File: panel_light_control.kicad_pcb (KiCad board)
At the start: 4 copper layers, 109 parts, among them J1 Conn_01x02, J11 RJ45_Shielded, J12 RJ45_Shielded, J13 HR911105A, J6 Conn_01x04, Q1 IRF540N, Q2 IRF540N, Q3 IRF540N, U1 L7805, U2 LM324, U3 STM32F207VGTx, U4 MCP2562-E-P, U5 LAN8720A, Y1 Crystal_GND24

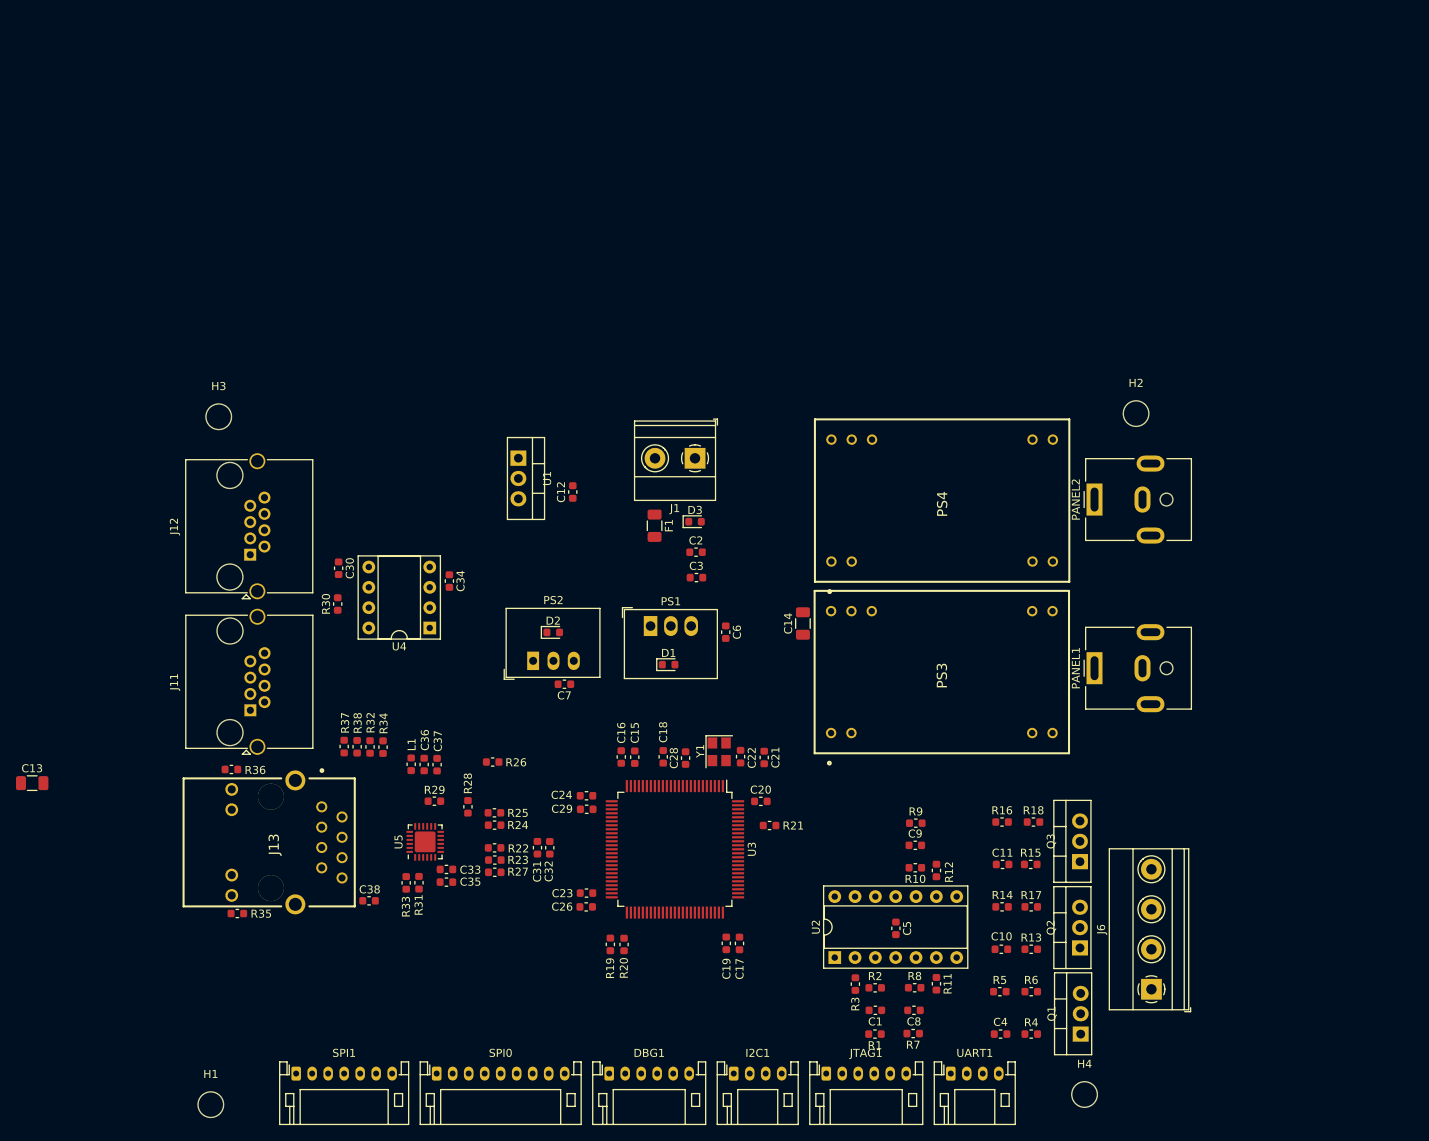
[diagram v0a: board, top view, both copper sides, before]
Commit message: PHY routing done? Current sink routing is back to square one (yay fwd annotations)
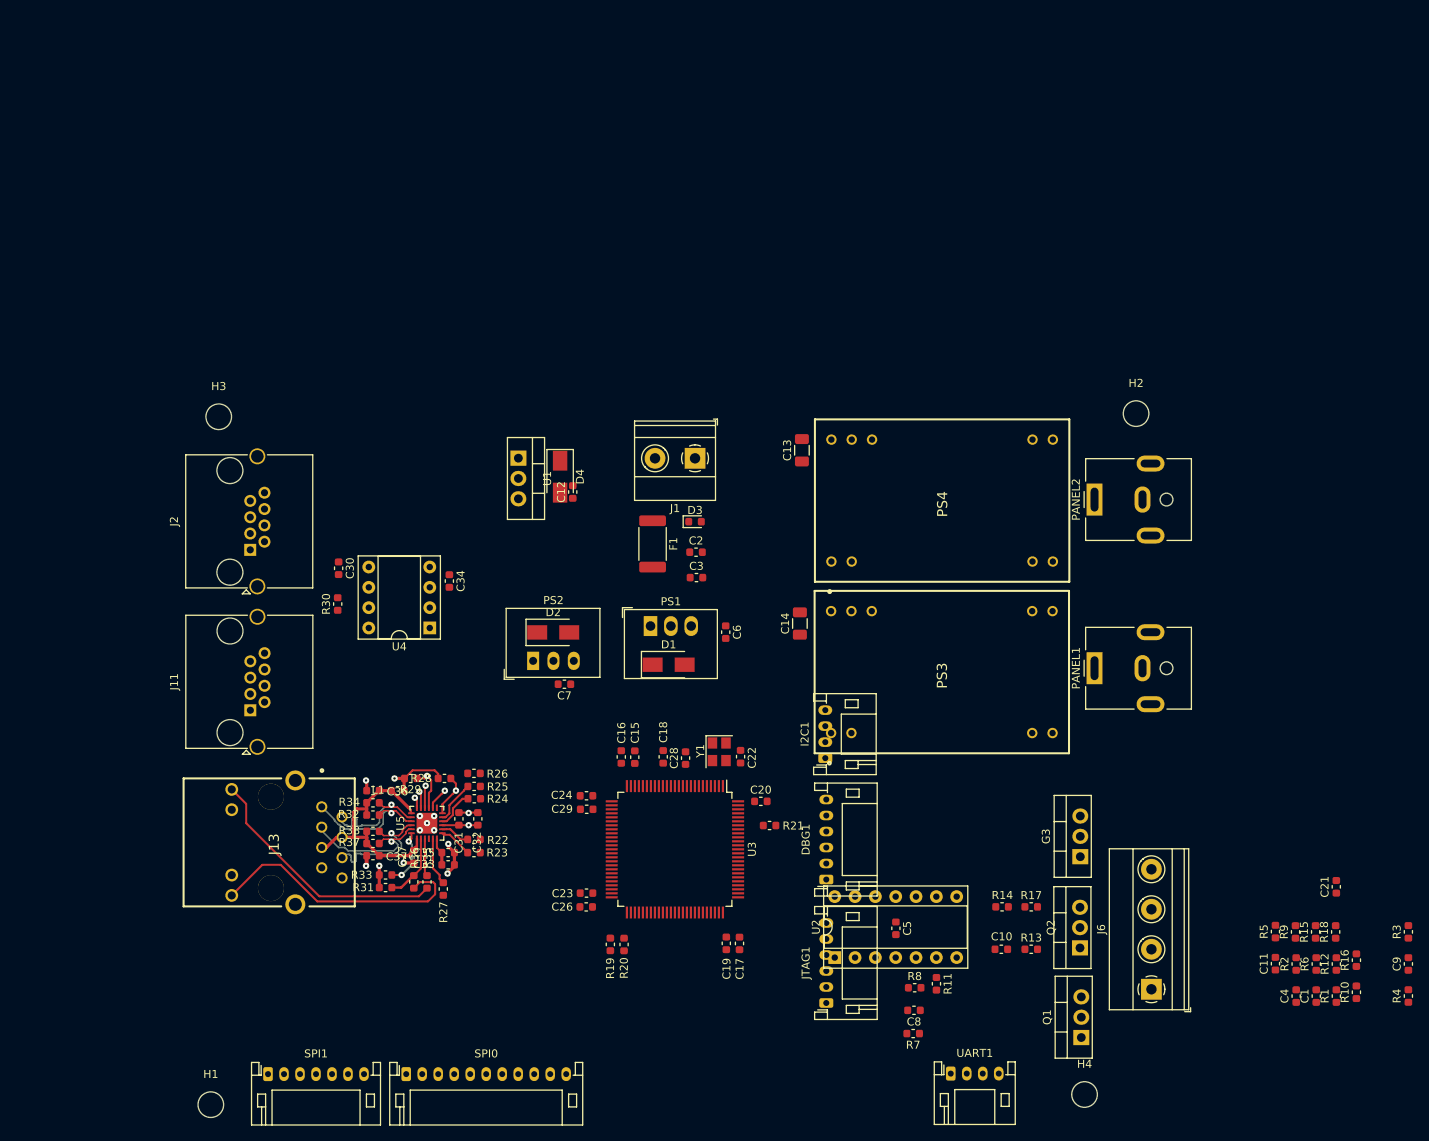
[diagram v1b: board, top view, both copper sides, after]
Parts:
- removed C38: 22nF, Capacitor_SMD:C_0603_1608Metric
- removed J12: RJ45_Shielded, Connector_RJ:RJ45_Amphenol_RJHSE5380
- removed Q3: IRF540N, Package_TO_SOT_THT:TO-220-3_Vertical
- added C27: 100nF, Capacitor_SMD:C_0603_1608Metric, F.Cu at (82.8, 129.9)
- added D4: D, Diode_SMD:D_SMA, F.Cu at (101.1, 82.4)
- added G3: IRF540N, Package_TO_SOT_THT:TO-220-3_Vertical, F.Cu at (166.1, 129.9)
- added J2: RJ45_Shielded, Connector_RJ:RJ45_Amphenol_RJHSE5380, F.Cu at (62.4, 91.6)
- C36, C37: value 104pF -> 100nF
- D1, D2: footprint Diode_SMD:D_0603_1608Metric -> Diode_SMD:D_SMA
- F1: footprint Fuse:Fuse_1206_3216Metric -> Fuse:Fuse_2512_6332Metric
- L1: value L -> FB
- SPI0: value Conn_01x09 -> Conn_01x10; footprint Connector_JST:JST_PH_S9B-PH-K_1x09_P2.00mm_Horizontal -> Connector_JST:JST_PH_S11B-PH-K_1x11_P2.00mm_Horizontal
- U3: value STM32F207VGTx -> STM32F207VGT6
- moved C13 104.8 mm to (131.3, 79.1), turned to 90 degrees
- moved C21 73.3 mm to (198.1, 133.7), turned to 90 degrees
- moved R3 69.4 mm to (207.1, 139.3), turned to 90 degrees
- moved C9 63.4 mm to (207.1, 143.3), turned to 90 degrees
- moved R1 57.9 mm to (198.1, 147.3), turned to 90 degrees
- moved R10 57.3 mm to (200.6, 146.9), turned to 90 degrees
- moved C1 55.1 mm to (195.6, 147.3), turned to 90 degrees
- moved R2 52.7 mm to (193.1, 143.3), turned to 90 degrees
- moved R12 51.3 mm to (198.1, 143.3)
- moved R9 49.4 mm to (193.0, 139.3), turned to 90 degrees
- moved R16 47.5 mm to (200.6, 142.9), turned to 90 degrees
- moved R4 47.4 mm to (207.1, 147.3), turned to 90 degrees
- moved I2C1 41.1 mm to (134.2, 117.6), turned to 90 degrees
- moved R18 40.2 mm to (198.0, 139.3), turned to 90 degrees
- moved C4 37.3 mm to (193.1, 147.3), turned to 90 degrees
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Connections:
- net /MCU/RX_N renamed RX_N
- net /MCU/RX_P renamed RX_P
- net /MCU/TX_N renamed TX_N
- net /MCU/TX_P renamed TX_P
- C21 pad 1: GND -> Net-(C21-Pad1)
- C21 pad 2: Net-(C21-Pad2) -> GND
- C31 pad 1: +3.3V -> GND
- C31 pad 2: GND -> +3.3V
- C32 pad 1: +3.3V -> GND
- C32 pad 2: GND -> +3.3V
- C33 pad 1: Net-(C33-Pad1) -> GND
- C33 pad 2: GND -> /MCU/VDDCR
- C35 pad 1: Net-(C33-Pad1) -> GND
- C35 pad 2: GND -> /MCU/VDDCR
- C36 pad 1: VDDA -> GND
- C36 pad 2: GND -> PHY_VDDA
- C37 pad 1: VDDA -> GND
- C37 pad 2: GND -> PHY_VDDA
- J13 pad 4: VDDA -> PHY_VDDA
- J13 pad 5: VDDA -> PHY_VDDA
- L1 pad 1: +3.3V -> PHY_VDDA
- L1 pad 2: VDDA -> +3.3V
- R1 pad 1: PWM_R -> Net-(C1-Pad2)
- R1 pad 2: Net-(C1-Pad2) -> PWM_R
- R14 pad 1: Net-(Q2-Pad3) -> Net-(C10-Pad2)
- R14 pad 2: Net-(C10-Pad2) -> Net-(Q2-Pad3)
- R16 pad 1: Net-(Q3-Pad3) -> Net-(C11-Pad2)
- R16 pad 2: Net-(C11-Pad2) -> Net-(G3-Pad3)
- R17 pad 1: GND -> Net-(Q2-Pad3)
- R17 pad 2: Net-(Q2-Pad3) -> GND
- R18 pad 1: GND -> Net-(G3-Pad3)
- R18 pad 2: Net-(Q3-Pad3) -> GND
- R32 pad 1: VDDA -> PHY_VDDA
- R34 pad 1: VDDA -> PHY_VDDA
- R37 pad 1: VDDA -> PHY_VDDA
- R38 pad 1: VDDA -> PHY_VDDA
- R5 pad 1: Net-(Q1-Pad3) -> Net-(C4-Pad2)
- R5 pad 2: Net-(C4-Pad2) -> Net-(Q1-Pad3)
- R6 pad 1: GND -> Net-(Q1-Pad3)
- R6 pad 2: Net-(Q1-Pad3) -> GND
- R7 pad 1: PWM_G -> Net-(C8-Pad2)
- R7 pad 2: Net-(C8-Pad2) -> PWM_G
- R9 pad 1: PWM_B -> Net-(C9-Pad2)
- R9 pad 2: Net-(C9-Pad2) -> PWM_B
- U3 pad 13: Net-(C21-Pad2) -> Net-(C21-Pad1)
- U5 pad 1: VDDA -> PHY_VDDA
- U5 pad 19: VDDA -> PHY_VDDA
- U5 pad 6: Net-(C33-Pad1) -> /MCU/VDDCR
- Y1 pad 1: Net-(C21-Pad2) -> Net-(C21-Pad1)
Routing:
- net LED_YLW-: track 0.00 -> 33.6 mm
- net LED_GRN-: track 0.00 -> 31.8 mm
- net PHY_VDDA: track 0.00 -> 31.4 mm
- net RX_P: track 0.00 -> 17.6 mm, vias 0 -> 1
- net RX_N: track 0.00 -> 17.2 mm, vias 0 -> 1
- net TX_P: track 0.00 -> 16.8 mm, vias 0 -> 1
- net TX_N: track 0.00 -> 15.8 mm, vias 0 -> 1
- net GND: track 0.00 -> 13.4 mm, vias 0 -> 12
- net +3.3V: track 0.00 -> 12.6 mm, vias 0 -> 2
- net Net-(R31-Pad1): track 0.00 -> 8.34 mm
- net Net-(R33-Pad1): track 0.00 -> 7.27 mm, vias 0 -> 2
- net Net-(R27-Pad1): track 0.00 -> 6.03 mm
- net LAN_RST: track 0.00 -> 5.69 mm, vias 0 -> 1
- net Net-(R25-Pad1): track 0.00 -> 5.40 mm
- net RMII_MDIO: track 0.00 -> 5.32 mm, vias 0 -> 1
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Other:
- net class Default: clearance 0.2 -> 0.15; trace_width 0.25 -> 0.2; via_drill 0.4 -> 0.3
- rule trace_clearance: 0.2 -> 0.15
- rule via_min_size: 0.4 -> 0.3

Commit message: further re-arrangement, PCB is now 100x90 mm² \o/. A bit more placement to do, then back to routing :>
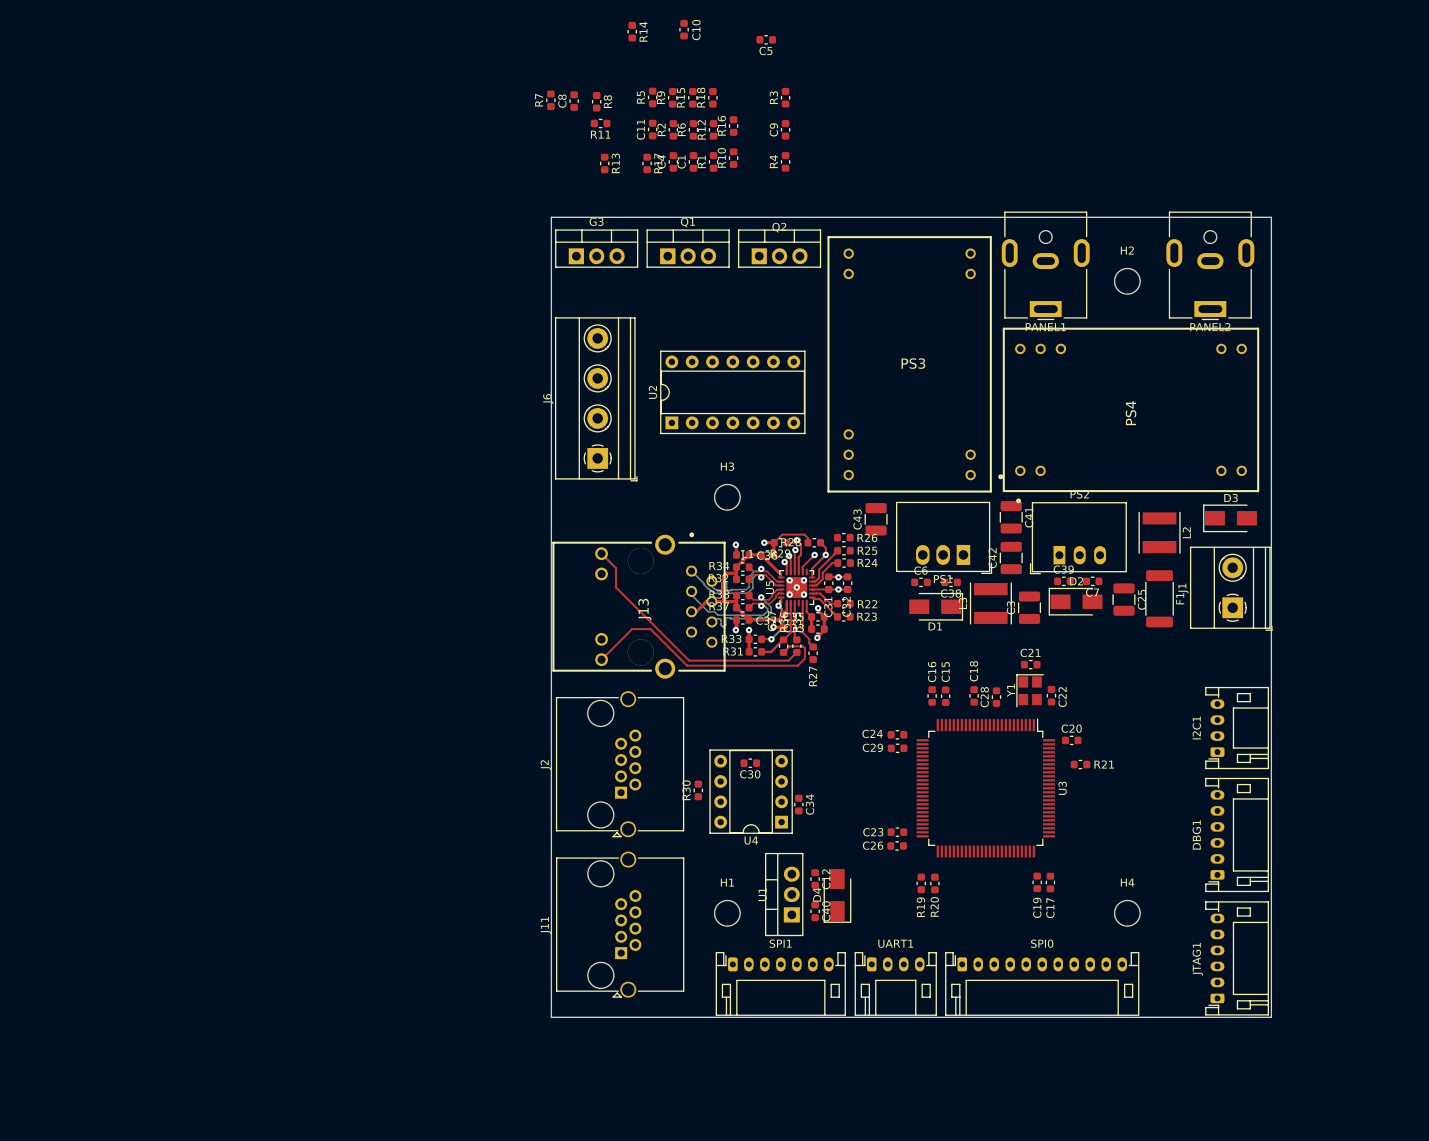
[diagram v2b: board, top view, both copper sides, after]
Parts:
- removed C13, C14: 4.7uF, Capacitor_SMD:C_1206_3216Metric
- removed C2: 100nF, Capacitor_SMD:C_0603_1608Metric
- added C25: 22µF, Capacitor_SMD:C_1210_3225Metric, F.Cu at (171.6, 97.8)
- added C38: 100nF, Capacitor_SMD:C_0603_1608Metric, F.Cu at (150.0, 95.6)
- added C39: 100nF, Capacitor_SMD:C_0603_1608Metric, F.Cu at (164.1, 95.5)
- added C40: 100nF, Capacitor_SMD:C_0603_1608Metric, F.Cu at (133.0, 136.8)
- added C41: 22µF, Capacitor_SMD:C_1210_3225Metric, F.Cu at (157.5, 87.5)
- added C42: 22µF, Capacitor_SMD:C_1210_3225Metric, F.Cu at (157.5, 92.6)
- added C43: 22µF, Capacitor_SMD:C_1210_3225Metric, F.Cu at (140.6, 87.8)
- added L2: 4.7µH, Inductor_SMD:L_Taiyo-Yuden_NR-50xx, F.Cu at (176.0, 89.4)
- added L3: 4.7µH, Inductor_SMD:L_Taiyo-Yuden_NR-50xx, F.Cu at (154.9, 98.3)
- C3: value 47uF -> 22µF; footprint Capacitor_SMD:C_0603_1608Metric -> Capacitor_SMD:C_1210_3225Metric
- D1, D2, D4: value D -> 1D4004
- D3: value D_Small -> 1D4004; footprint Diode_SMD:D_0603_1608Metric -> Diode_SMD:D_SMA
- moved C11 130.1 mm to (112.7, 39.0)
- moved C4 130.1 mm to (115.2, 43.1)
- moved C9 130.1 mm to (129.3, 39.1)
- moved R10 130.1 mm to (122.8, 42.6)
- moved R16 130.1 mm to (122.8, 38.6)
- moved R18 130.1 mm to (120.2, 35.1)
- moved R2 130.1 mm to (115.2, 39.1)
- moved R5 130.1 mm to (112.7, 35.0)
- moved C1 130.1 mm to (117.8, 43.1)
- moved R1 130.1 mm to (120.3, 43.1)
- moved R12 130.1 mm to (120.3, 39.1)
- moved R15 130.1 mm to (117.7, 35.1)
- moved R3 130.1 mm to (129.3, 35.1)
- moved R4 130.1 mm to (129.3, 43.1)
- moved R6 130.1 mm to (117.8, 39.1)
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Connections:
- D1 pad 1: +24V -> Net-(C38-Pad1)
- D2 pad 1: +24V -> Net-(C39-Pad1)
- PS1 pad 1: +24V -> Net-(C38-Pad1)
- PS2 pad 1: +24V -> Net-(C39-Pad1)
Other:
- board outline added: 90 x 100 mm

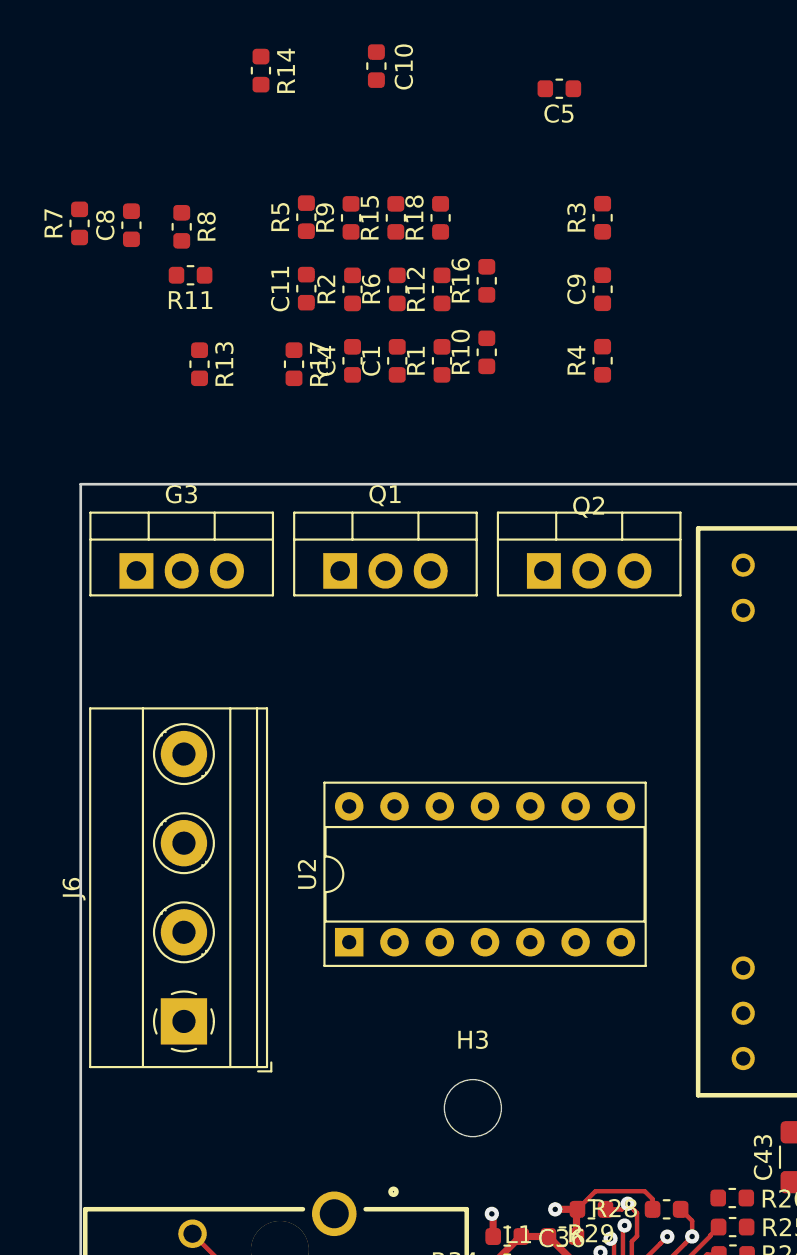
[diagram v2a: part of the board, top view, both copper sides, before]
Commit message: Tweaked LED sink layout, fixed 3D model for 1 RJ45 jack.
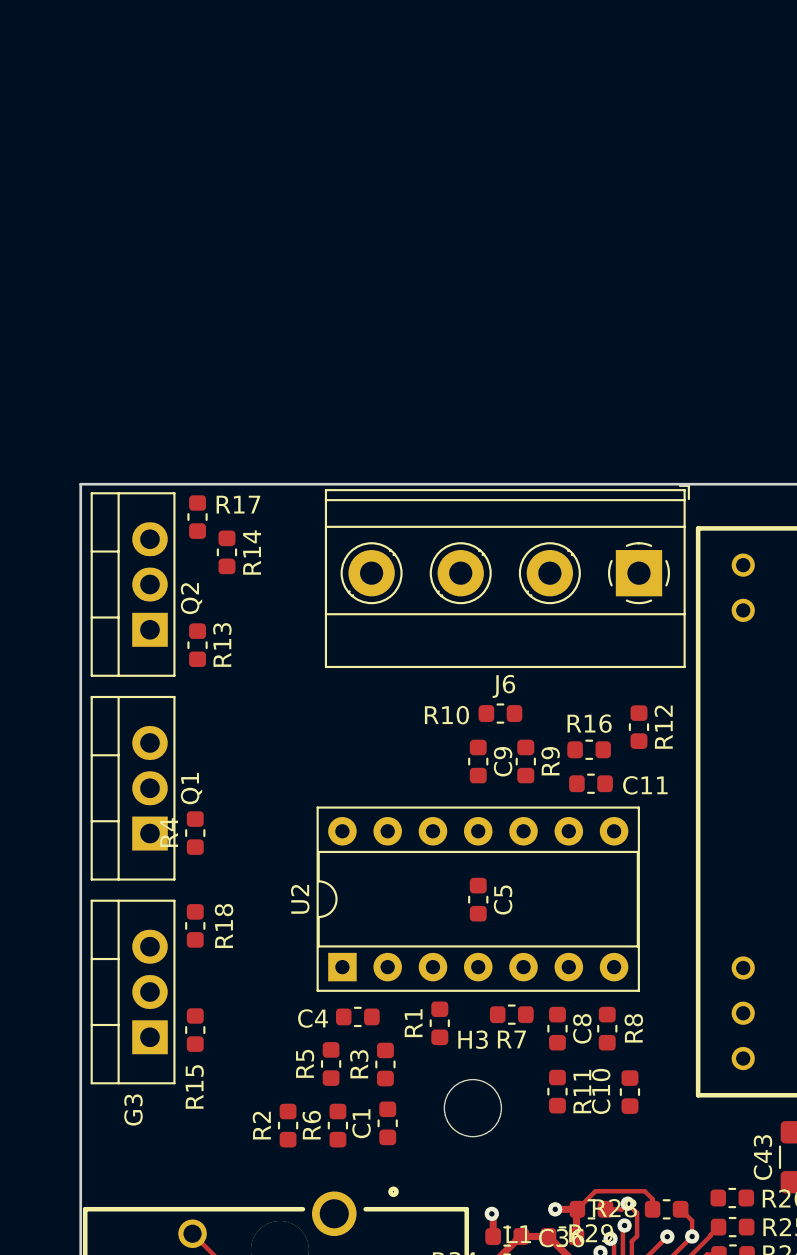
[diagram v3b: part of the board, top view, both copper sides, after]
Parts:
- moved C10 59.3 mm to (130.8, 84.1), turned to 270 degrees
- moved C8 51.0 mm to (126.7, 80.5), turned to 270 degrees
- moved R8 50.9 mm to (129.5, 80.5), turned to 90 degrees
- moved R7 50.6 mm to (124.2, 79.8), turned to 180 degrees
- moved R11 50.2 mm to (126.7, 84.1), turned to 270 degrees
- moved R3 49.0 mm to (117.1, 82.5)
- moved R5 47.5 mm to (114.0, 82.5)
- moved R2 47.0 mm to (111.6, 86.0)
- moved R6 47.0 mm to (114.4, 86.0)
- moved R15 46.9 mm to (106.4, 80.6)
- moved C5 45.7 mm to (122.3, 73.3), turned to 270 degrees
- moved C1 42.8 mm to (117.2, 85.9)
- moved R18 42.0 mm to (106.4, 74.8)
- moved R1 37.2 mm to (120.1, 80.2)
- moved C4 36.8 mm to (115.5, 79.9), turned to 180 degrees
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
